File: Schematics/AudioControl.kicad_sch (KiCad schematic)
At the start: 1 part, among them J127 AudioJack1

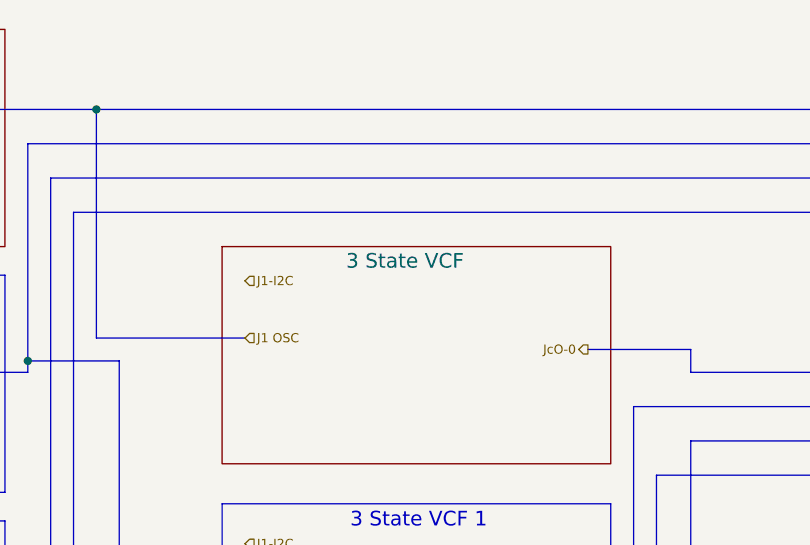
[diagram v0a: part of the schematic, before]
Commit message: Finalized first filter design.  Setep for filter testing.
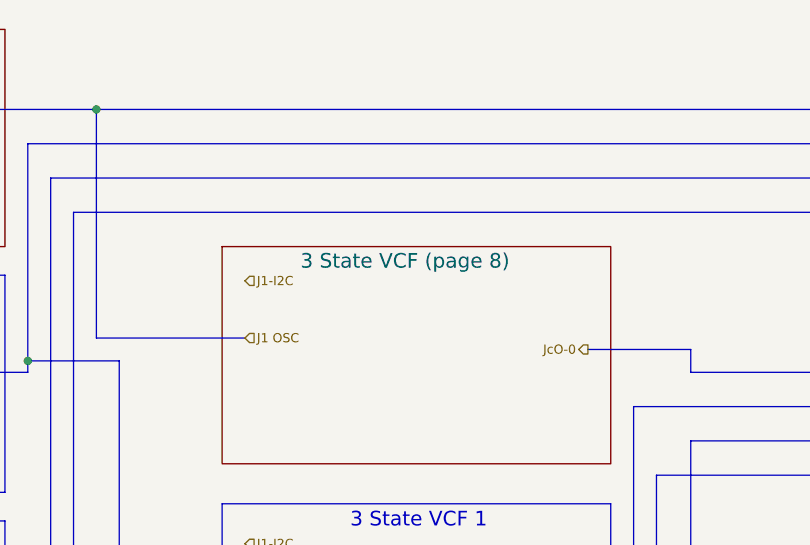
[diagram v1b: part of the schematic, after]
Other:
- sheet 3 State VCF renamed 3 State VCF (page 8)
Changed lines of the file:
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@@
 			(color 0 0 0 0.0000)
 		)
-		(property "Sheetname" "3 State VCF"
+		(property "Sheetname" "3 State VCF (page 8)"
 			(at 195.58 44.45 0)
 			(effects

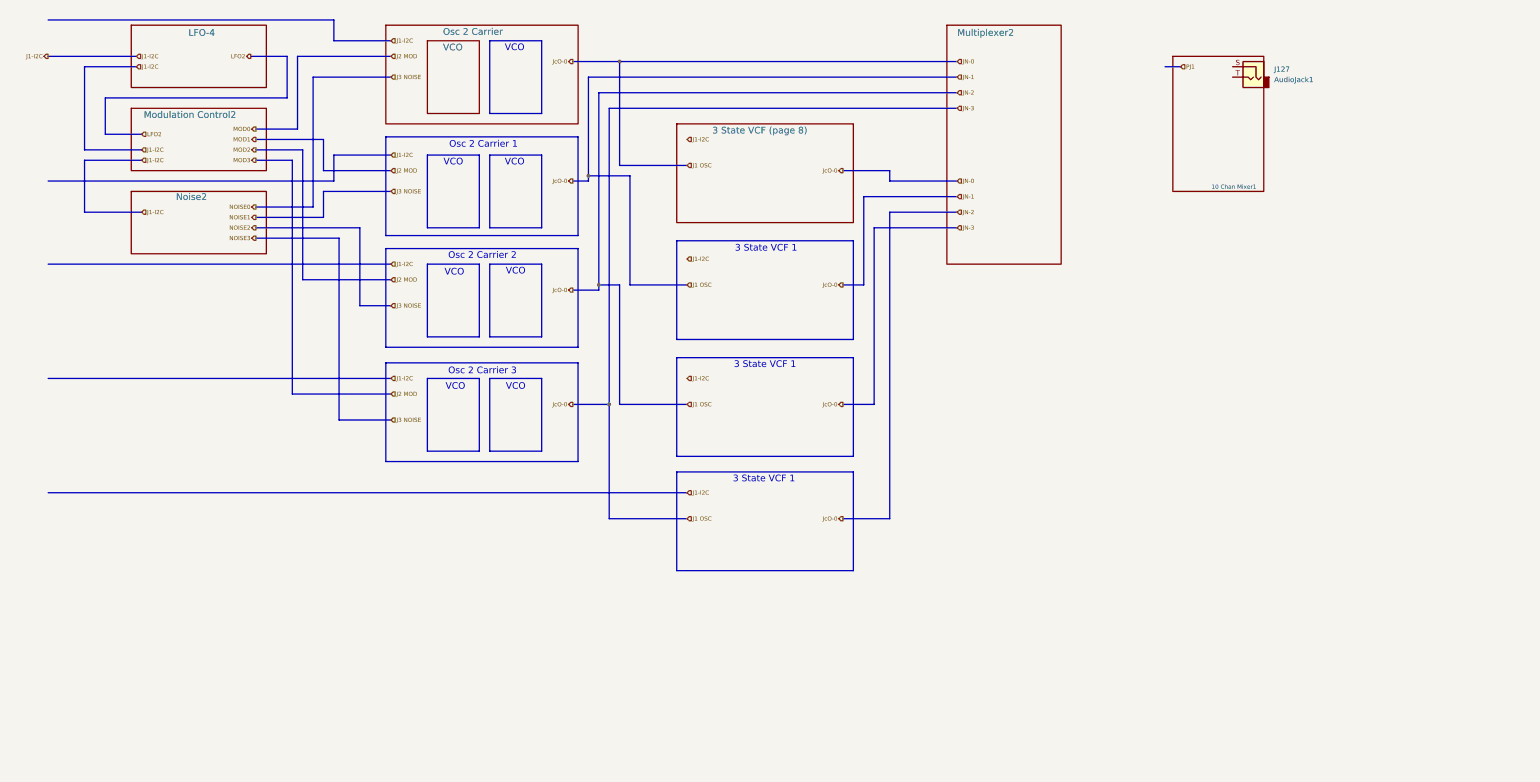
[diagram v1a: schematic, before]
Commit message: Fixed schematic errors.
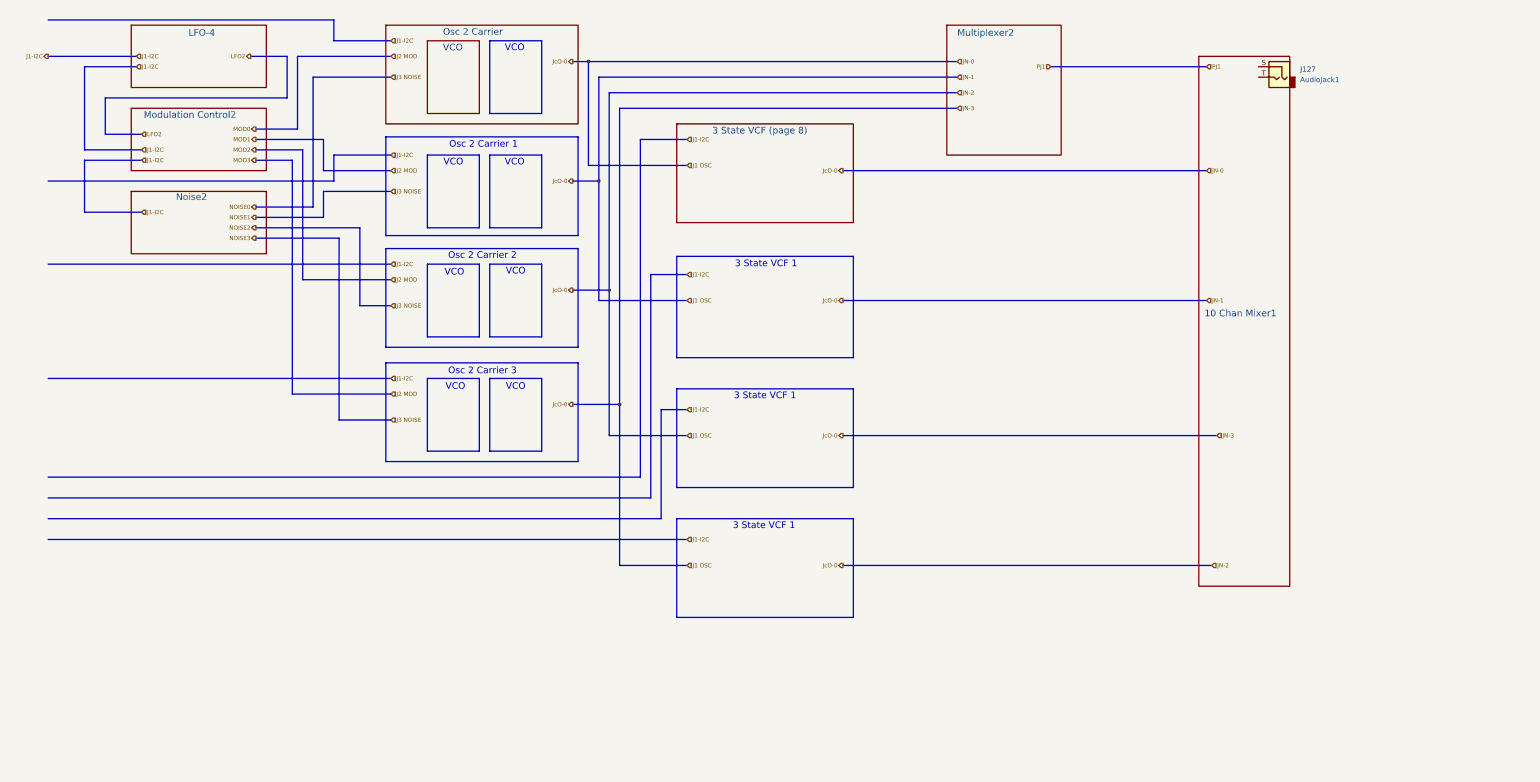
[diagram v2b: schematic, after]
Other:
- moved on the sheet: J127

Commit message: New output mixer with VCAs
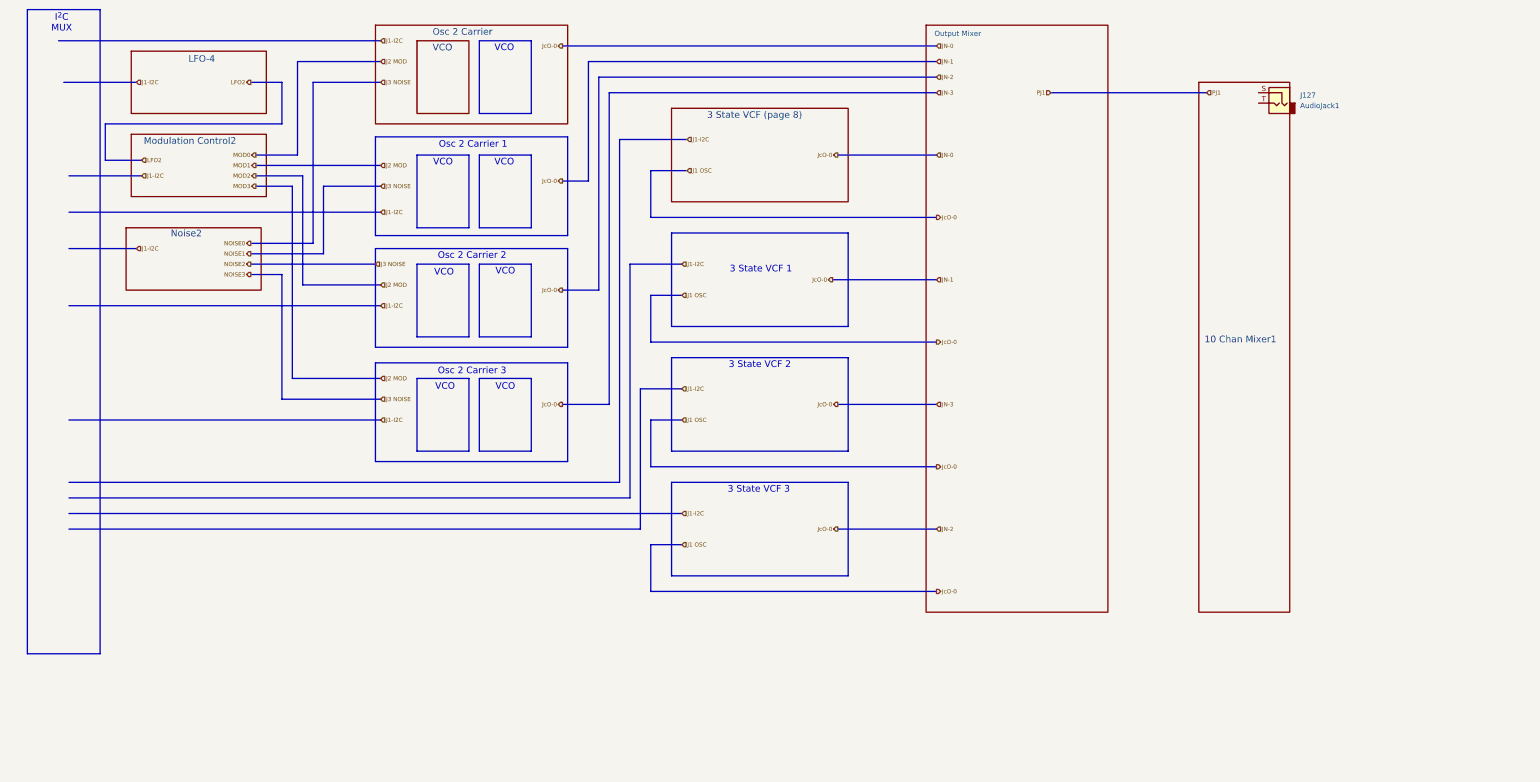
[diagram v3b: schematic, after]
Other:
- removed sheet Multiplexer2
- added sheet Output Mixer (OutputMIX.kicad_sch)
- note added: "3 State VCF 2"
- note added: "3 State VCF 3"
- note added: "I^{2}C MUX"
- moved on the sheet: J127

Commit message: Updated schematics.  Added modulation control to VCF.
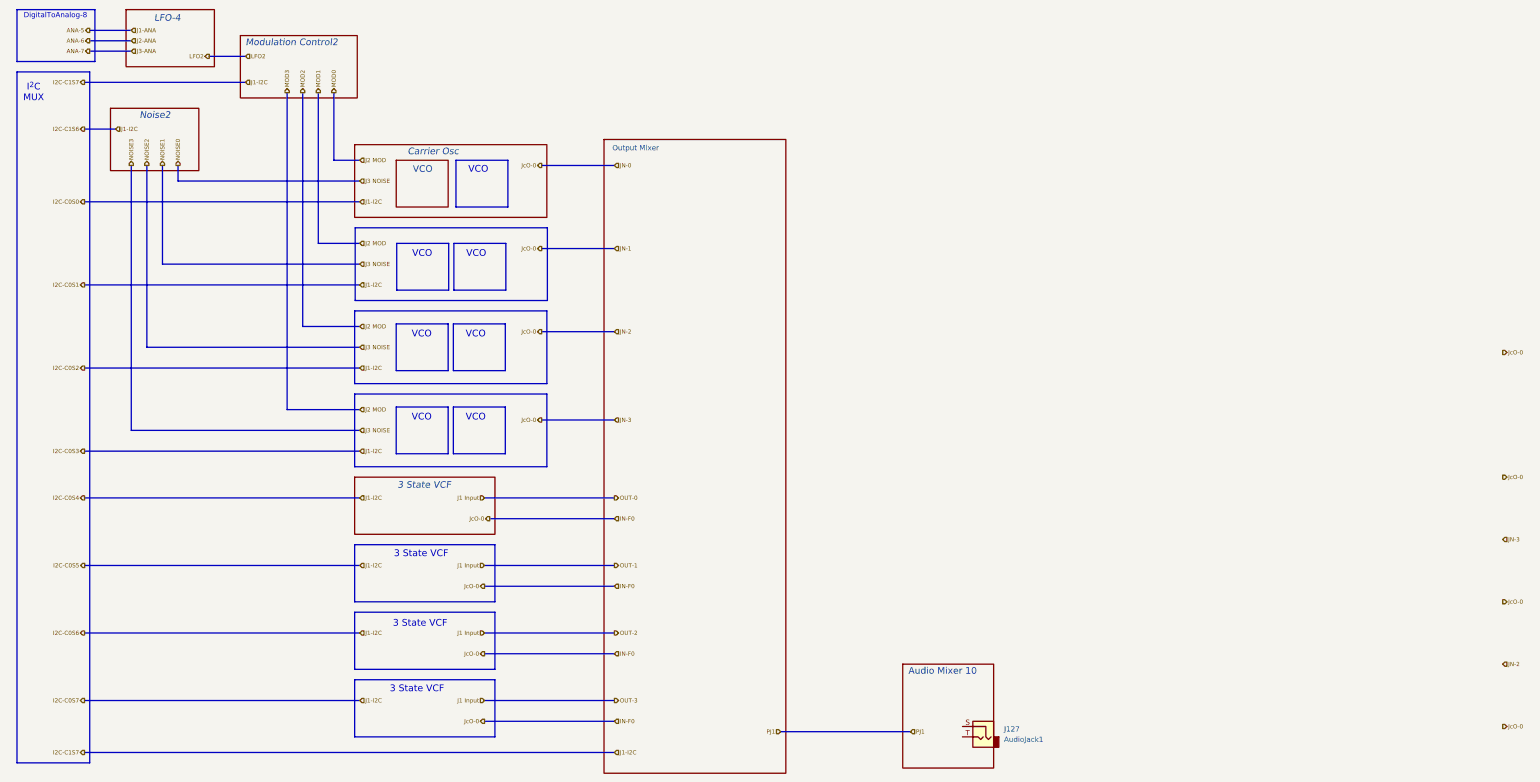
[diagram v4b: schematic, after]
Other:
- sheet 10 Chan Mixer1 renamed Audio Mixer 10
- sheet 3 State VCF (page 8) renamed 3 State VCF
- sheet Osc 2 Carrier renamed Carrier Osc
- note added: "3 State VCF"
- note added: "DigitalToAnalog-8"
- note removed: "3 State VCF 1"
- note removed: "3 State VCF 2"
- note removed: "3 State VCF 3"
- note removed: "Osc 2 Carrier 1"
- note removed: "Osc 2 Carrier 2"
- note removed: "Osc 2 Carrier 3"
- moved on the sheet: J127

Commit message: Updated schematics and added low pass filter and new filter mux.
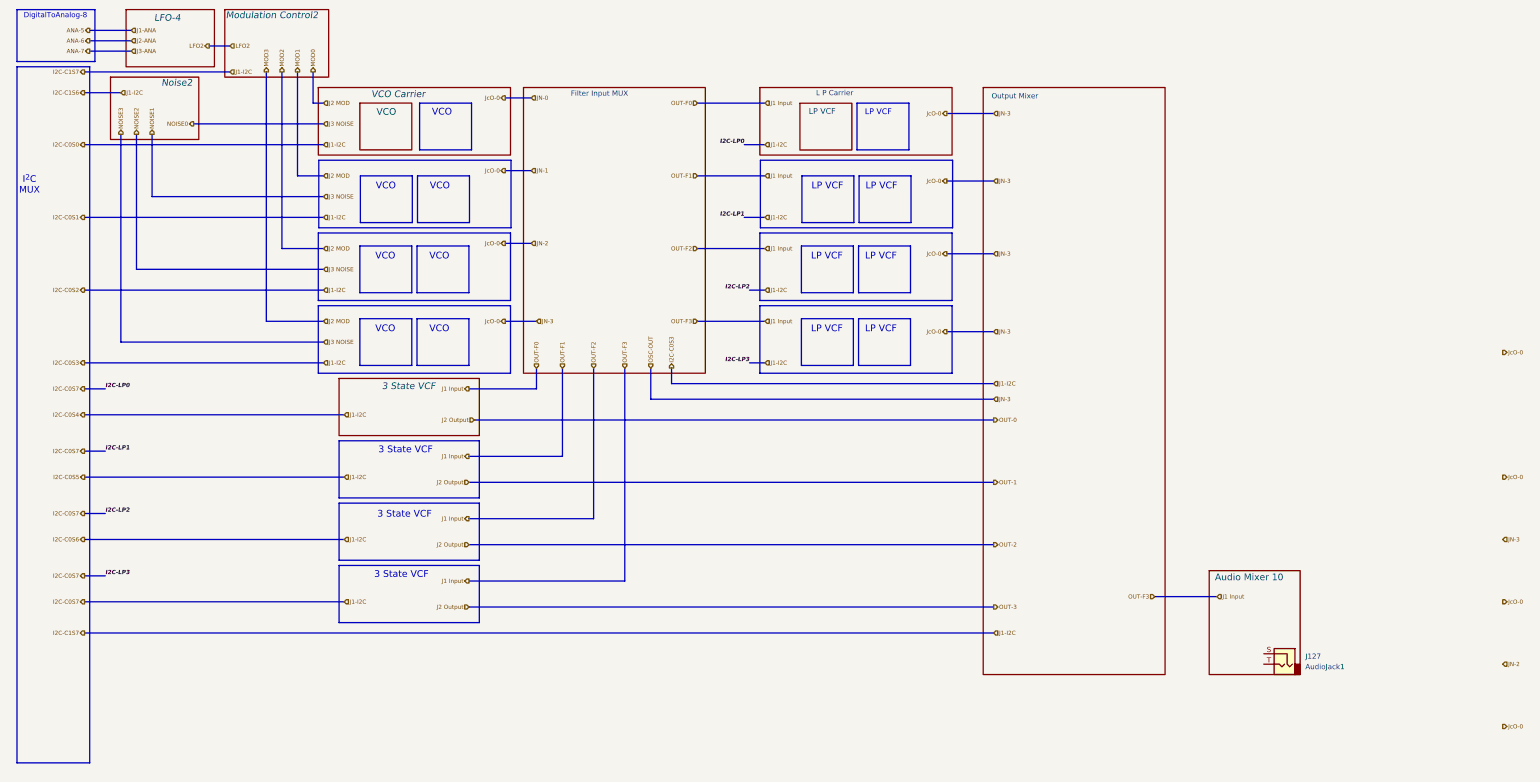
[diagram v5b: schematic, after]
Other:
- sheet Carrier Osc renamed VCO Carrier
- added sheet Filter Input MUX (FilterInputMux.kicad_sch)
- added sheet L P Carrier (LPcarrier.kicad_sch)
- added sheet LP VCF (LowPassFilter.kicad_sch)
- note added: "LP VCF"
- moved on the sheet: J127

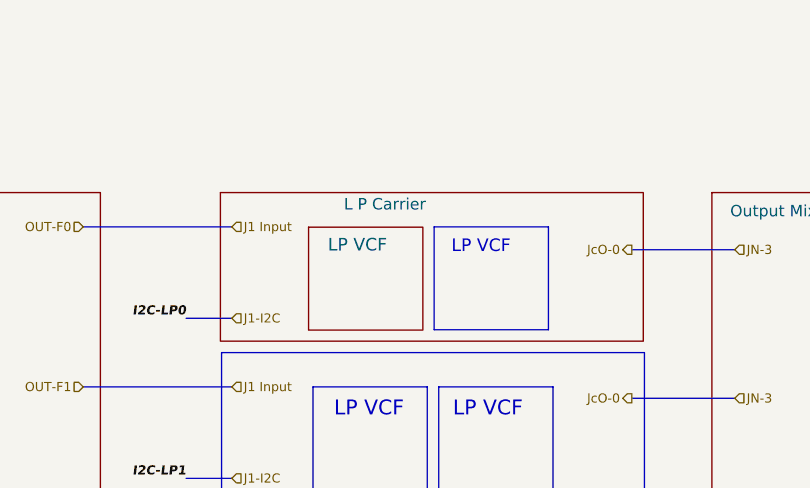
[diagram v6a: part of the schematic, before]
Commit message: Updated schematics, adding new low pass fillter and, added some statistical synth data to monitor.
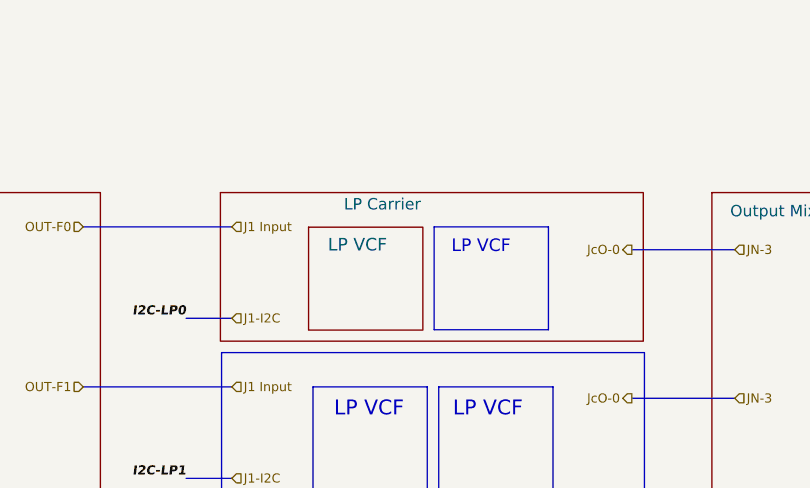
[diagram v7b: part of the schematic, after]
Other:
- sheet L P Carrier renamed LP Carrier
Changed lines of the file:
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@@
 	(paper "USLegal")
 	(title_block
-		(date "2025-11-28")
+		(date "2025-12-06")
 	)
 	(rectangle
@@
 			(color 0 0 0 0.0000)
 		)
-		(property "Sheetname" "L P Carrier"
+		(property "Sheetname" "LP Carrier"
 			(at 209.296 35.052 0)
 			(effects
